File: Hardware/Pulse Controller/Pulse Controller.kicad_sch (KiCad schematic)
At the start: 35 parts, among them J1 Serial, J2 RGB LED, J3 Arduino Out 1, J4 Arduino Out 2, J5 MOSFET Gates, J6 Signal In, P1 Power In, P2 PushButton, U1 ZSR330GTA, U2 ZSR500GTA, U3 4N35, U4 23LC1024, U5 LTC1855

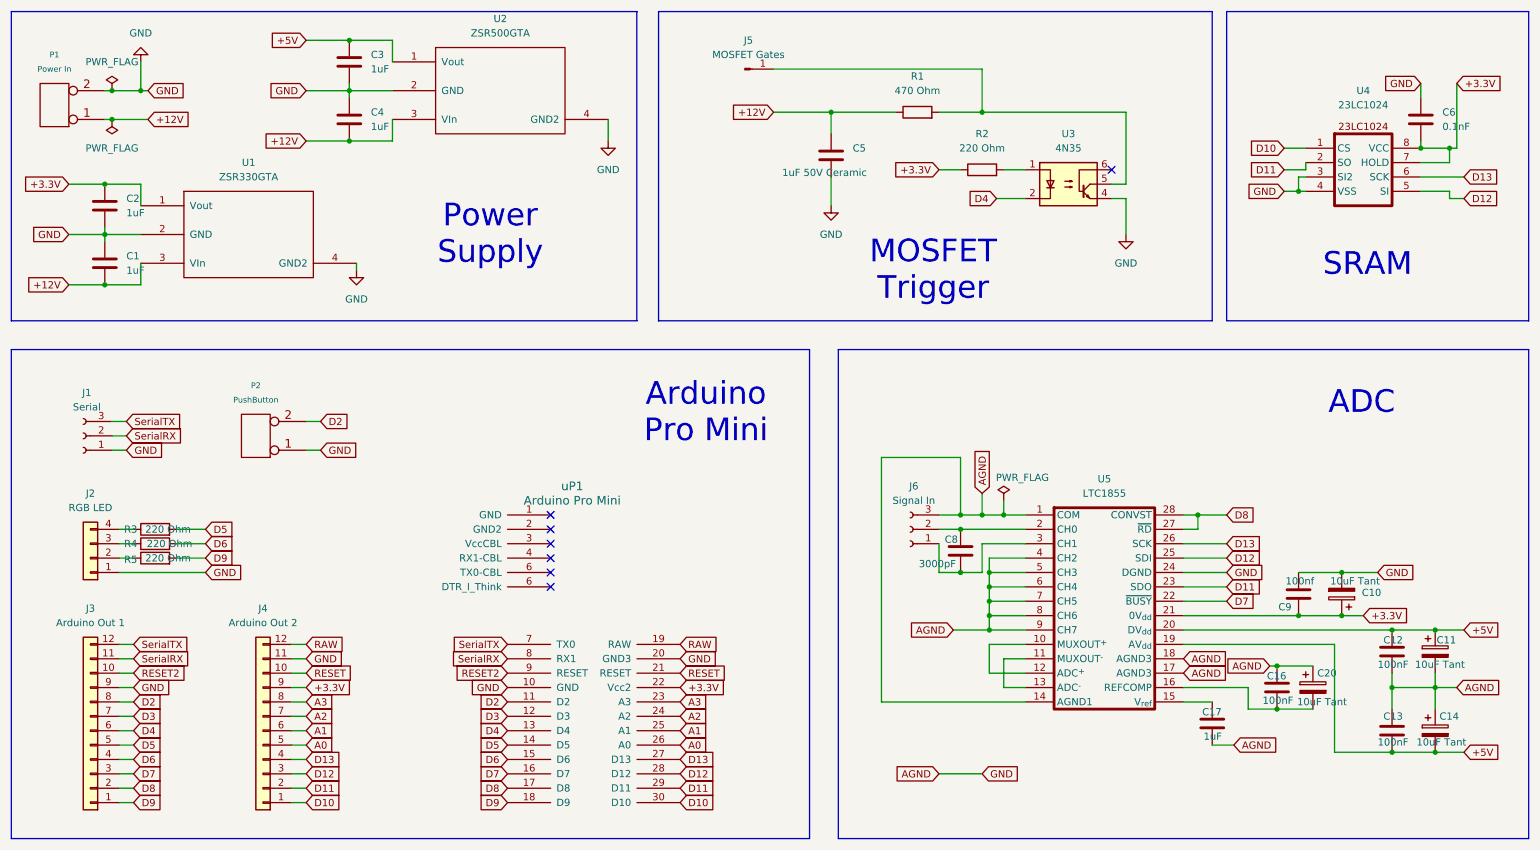
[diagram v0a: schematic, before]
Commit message: Changed some Caps to SMD
Also fixed MISO and MOSI assignments
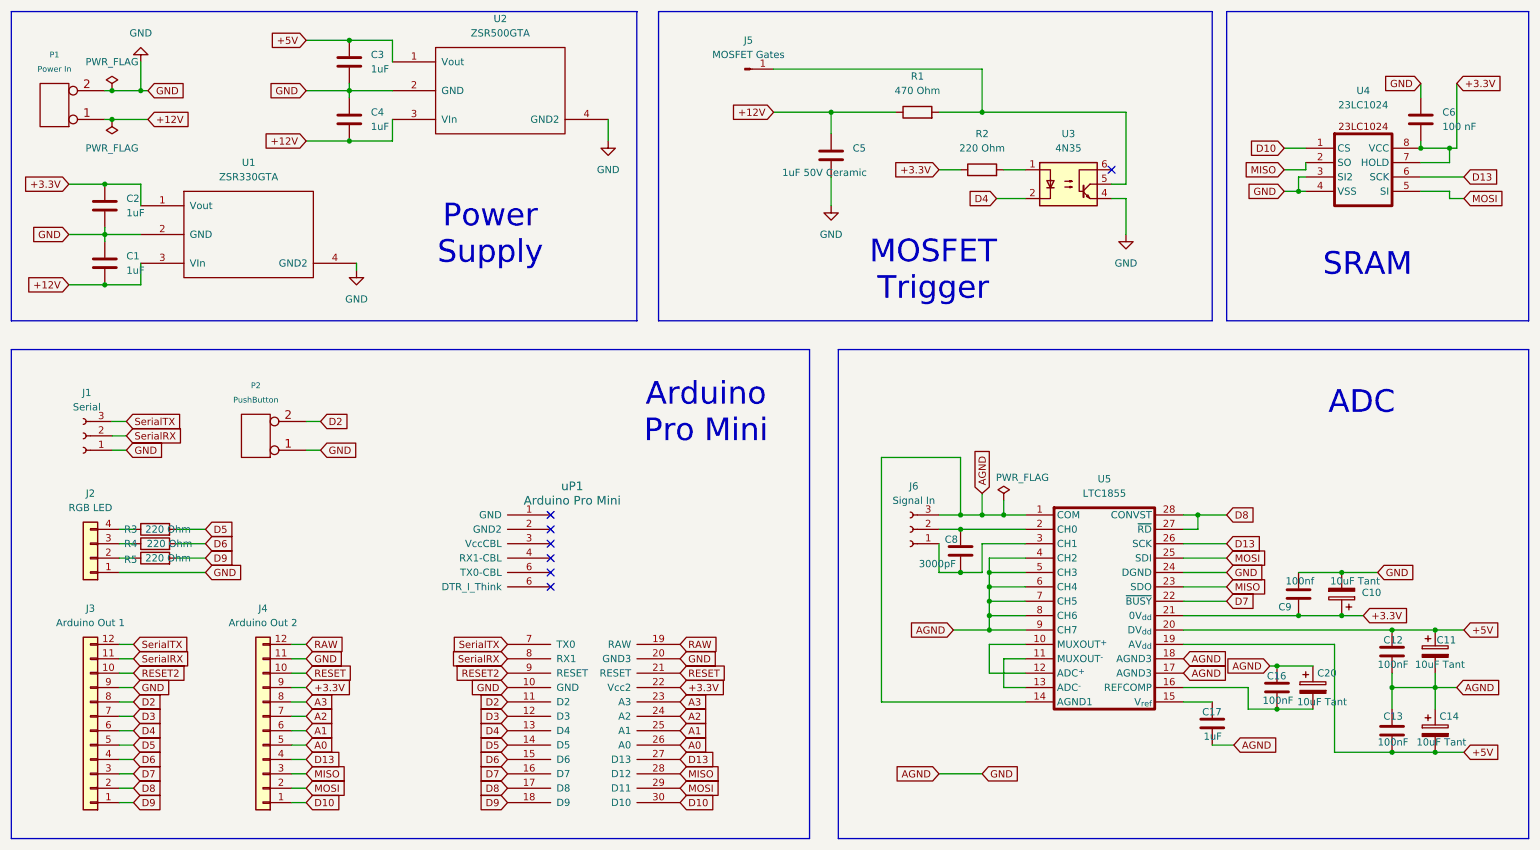
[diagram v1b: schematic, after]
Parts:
- C10, C11, C14, C20: footprint Capacitor_THT:C_Disc_D5.0mm_W2.5mm_P2.50mm -> Capacitor_SMD:C_1206_3216Metric_Pad1.33x1.80mm_HandSolder
- C5: footprint Capacitor_THT:C_Disc_D5.0mm_W2.5mm_P2.50mm -> Capacitor_SMD:C_0805_2012Metric_Pad1.18x1.45mm_HandSolder
- C6: value 0.1nF -> 100 nF
- R1: footprint Resistor_THT:R_Axial_DIN0207_L6.3mm_D2.5mm_P7.62mm_Horizontal -> Resistor_THT:R_Axial_DIN0309_L9.0mm_D3.2mm_P12.70mm_Horizontal
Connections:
- net D11 renamed MISO
- net MISO: now also J4.3 (Pin_3), uP1.28 (D12); no longer J4.2 (Pin_2), uP1.29 (D11)
- net D12 renamed MOSI
- net MOSI: now also J4.2 (Pin_2), uP1.29 (D11); no longer J4.3 (Pin_3), uP1.28 (D12)
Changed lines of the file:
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@@
 		)
 	)
-	(global_label "D11"
+	(global_label "MOSI"
 		(shape input)
 		(at 67.31 153.67 0)
@@
 		)
 		(property "Intersheetrefs" "${INTERSHEET_REFS}"
-			(at 73.9842 153.67 0)
+			(at 74.8914 153.67 0)
 			(effects
 				(font
@@
 		)
 	)
-	(global_label "D12"
+	(global_label "MOSI"
 		(shape input)
 		(at 229.87 113.03 0)
@@
 		)
 		(property "Intersheetrefs" "${INTERSHEET_REFS}"
-			(at 236.5442 113.03 0)
+			(at 237.4514 113.03 0)
 			(effects
 				(font
@@
 		)
 	)
-	(global_label "D12"
+	(global_label "MISO"
 		(shape input)
 		(at 67.31 151.13 0)
@@
 		)
 		(property "Intersheetrefs" "${INTERSHEET_REFS}"
-			(at 73.9842 151.13 0)
+			(at 74.8914 151.13 0)
 			(effects
 				(font
@@
 		)
 	)
-	(global_label "D11"
+	(global_label "MISO"
 		(shape input)
 		(at 240.03 44.45 180)
@@
 		)
 		(property "Intersheetrefs" "${INTERSHEET_REFS}"
-			(at 233.3558 44.45 0)
+			(at 232.4486 44.45 0)
 			(effects
 				(font
@@
 		)
 	)
-	(global_label "D12"
+	(global_label "MOSI"
 		(shape input)
 		(at 271.78 49.53 0)
@@
 		)
 		(property "Intersheetrefs" "${INTERSHEET_REFS}"
-			(at 278.4542 49.53 0)
+			(at 279.3614 49.53 0)
 			(effects
 				(font
@@
 		)
 	)
-	(global_label "D11"
+	(global_label "MOSI"
 		(shape input)
 		(at 133.35 153.67 0)
@@
 		)
 		(property "Intersheetrefs" "${INTERSHEET_REFS}"
-			(at 140.0242 153.67 0)
+			(at 140.9314 153.67 0)
 			(effects
 				(font
@@
 		)
 	)
-	(global_label "D11"
+	(global_label "MISO"
 		(shape input)
 		(at 229.87 118.11 0)
@@
 		)
 		(property "Intersheetrefs" "${INTERSHEET_REFS}"
-			(at 236.5442 118.11 0)
+			(at 237.4514 118.11 0)
 			(effects
 				(font
@@
 		)
 	)
-	(global_label "D12"
+	(global_label "MISO"
 		(shape input)
 		(at 133.35 151.13 0)
@@
 		)
 		(property "Intersheetrefs" "${INTERSHEET_REFS}"
-			(at 140.0242 151.13 0)
+			(at 140.9314 151.13 0)
 			(effects
 				(font
@@
 			)
 		)
-		(property "Footprint" "Resistor_THT:R_Axial_DIN0207_L6.3mm_D2.5mm_P7.62mm_Horizontal"
+		(property "Footprint" "Resistor_THT:R_Axial_DIN0309_L9.0mm_D3.2mm_P12.70mm_Horizontal"
 			(at 175.26 36.068 90)
 			(effects
@@
 			)
 		)
-		(property "Footprint" "Capacitor_THT:C_Disc_D5.0mm_W2.5mm_P2.50mm"
+		(property "Footprint" "Capacitor_SMD:C_1206_3216Metric_Pad1.33x1.80mm_HandSolder"
 			(at 267.6652 133.35 0)
 			(effects
@@
 			)
 		)
-		(property "Footprint" "Capacitor_THT:C_Disc_D5.0mm_W2.5mm_P2.50mm"
+		(property "Footprint" "Capacitor_SMD:C_1206_3216Metric_Pad1.33x1.80mm_HandSolder"
 			(at 249.2248 115.57 0)
 			(effects
@@
 			)
 		)
-		(property "Value" "0.1nF"
+		(property "Value" "100 nF"
 			(at 267.97 36.8299 0)
 			(effects
@@
 			)
 		)
-		(property "Footprint" "Capacitor_THT:C_Disc_D5.0mm_W2.5mm_P2.50mm"
+		(property "Footprint" "Capacitor_SMD:C_0805_2012Metric_Pad1.18x1.45mm_HandSolder"
 			(at 160.9852 45.72 0)
 			(effects
@@
 			)
 		)
-		(property "Footprint" "Capacitor_THT:C_Disc_D5.0mm_W2.5mm_P2.50mm"
+		(property "Footprint" "Capacitor_SMD:C_1206_3216Metric_Pad1.33x1.80mm_HandSolder"
 			(at 267.6652 147.32 0)
 			(effects
@@
 			)
 		)
-		(property "Footprint" "Capacitor_THT:C_Disc_D5.0mm_W2.5mm_P2.50mm"
+		(property "Footprint" "Capacitor_SMD:C_1206_3216Metric_Pad1.33x1.80mm_HandSolder"
 			(at 246.0752 139.7 0)
 			(effects

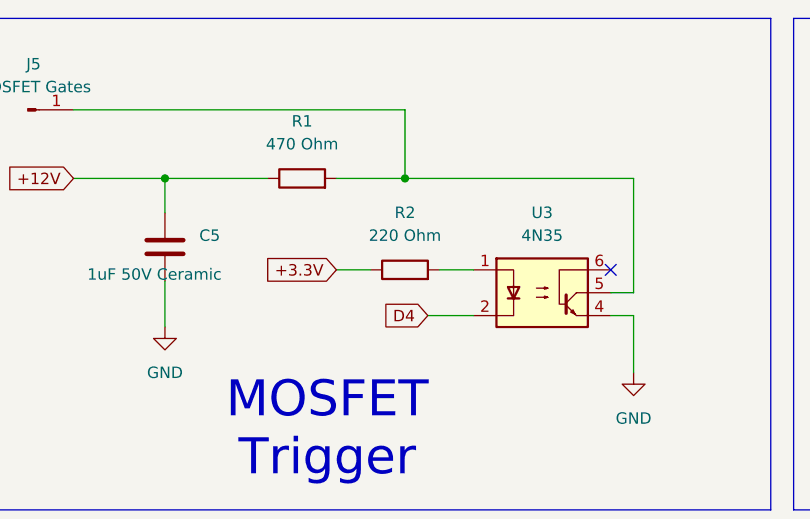
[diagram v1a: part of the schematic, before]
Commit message: PCB for Pulse Controller
First complete schematic for Amplifier
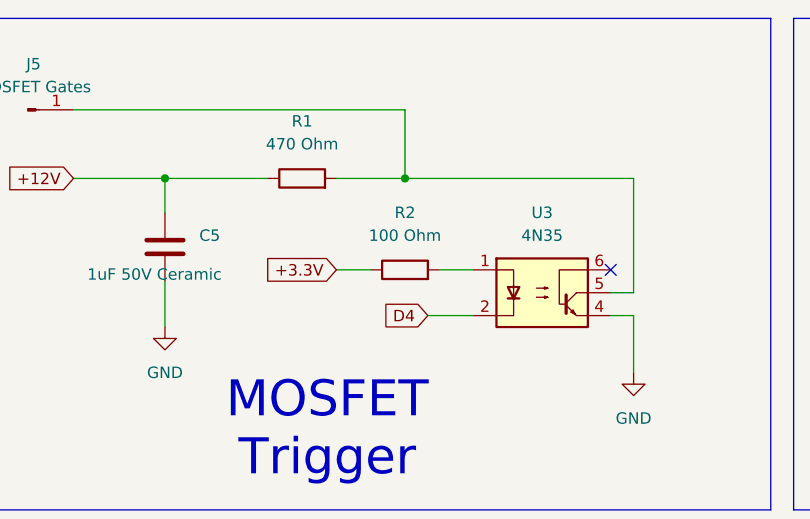
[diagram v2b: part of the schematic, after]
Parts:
- J5: footprint Connector_PinHeader_2.54mm:PinHeader_1x01_P2.54mm_Horizontal -> Connector_PinHeader_2.54mm:PinHeader_1x01_P2.54mm_Vertical
- R2: value 220 Ohm -> 100 Ohm
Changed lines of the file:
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@@
 			)
 		)
-		(property "Footprint" "Connector_PinHeader_2.54mm:PinHeader_1x01_P2.54mm_Horizontal"
+		(property "Footprint" "Connector_PinHeader_2.54mm:PinHeader_1x01_P2.54mm_Vertical"
 			(at 144.78 26.67 0)
 			(effects
@@
 			)
 		)
-		(property "Value" "220 Ohm"
+		(property "Value" "100 Ohm"
 			(at 186.69 40.64 90)
 			(effects
